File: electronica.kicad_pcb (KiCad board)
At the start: 2 copper layers, 100 x 100 mm, 56 parts, among them J1 Conn_02x02_Counter_Clockwise, J2 Raspberry_Pi_4, J3 Conn_01x12, J4 Conn_01x05, P1 Conn_01x03_Socket, P2 Conn_01x03_Socket, P3 Conn_01x03_Socket, P4 Conn_01x03_Socket, U1 ADS1115 MOD, U2 ULN2003AID

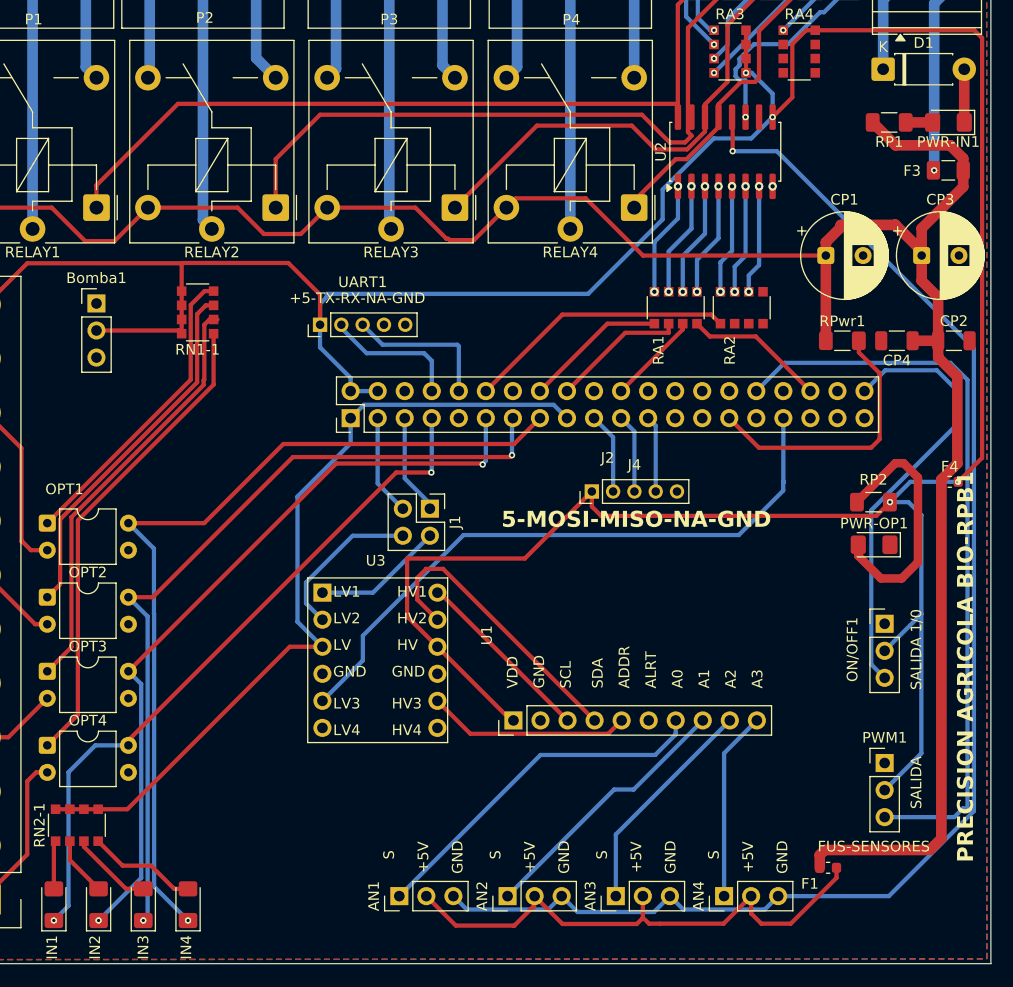
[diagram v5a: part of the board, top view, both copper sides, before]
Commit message: permanece un warning pero no deberia dar problemas4
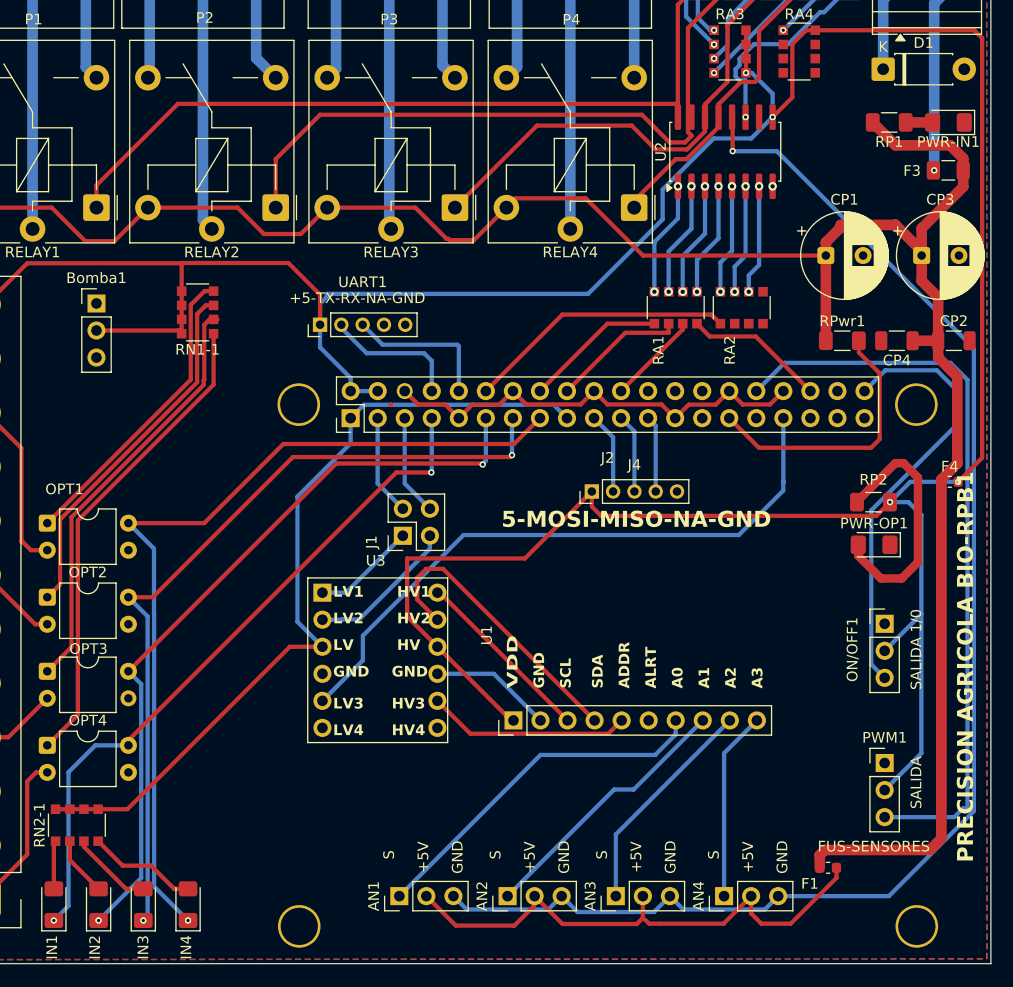
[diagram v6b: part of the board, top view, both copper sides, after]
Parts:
- moved J1 3.59 mm to (84.8, 107.3), turned to 90 degrees
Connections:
- J1 pad 2: Net-(J1-Pin_2) -> IO02-SDA
- J1 pad 3: IO02-SDA -> Net-(J1-Pin_2)
- J2 pad 40: unconnected-(J2-GPIO21/SPI1_SCLK/PCM_DOUT-Pad40) -> IO40
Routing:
- net GND: track 5.00 -> 53.5 mm
- net IO40: track 0.00 -> 41.4 mm
- net (no net): track 41.4 -> 0.00 mm
- net Net-(J1-Pin_1): track 12.3 -> 9.77 mm
- net Net-(J1-Pin_2): track 15.1 -> 14.1 mm

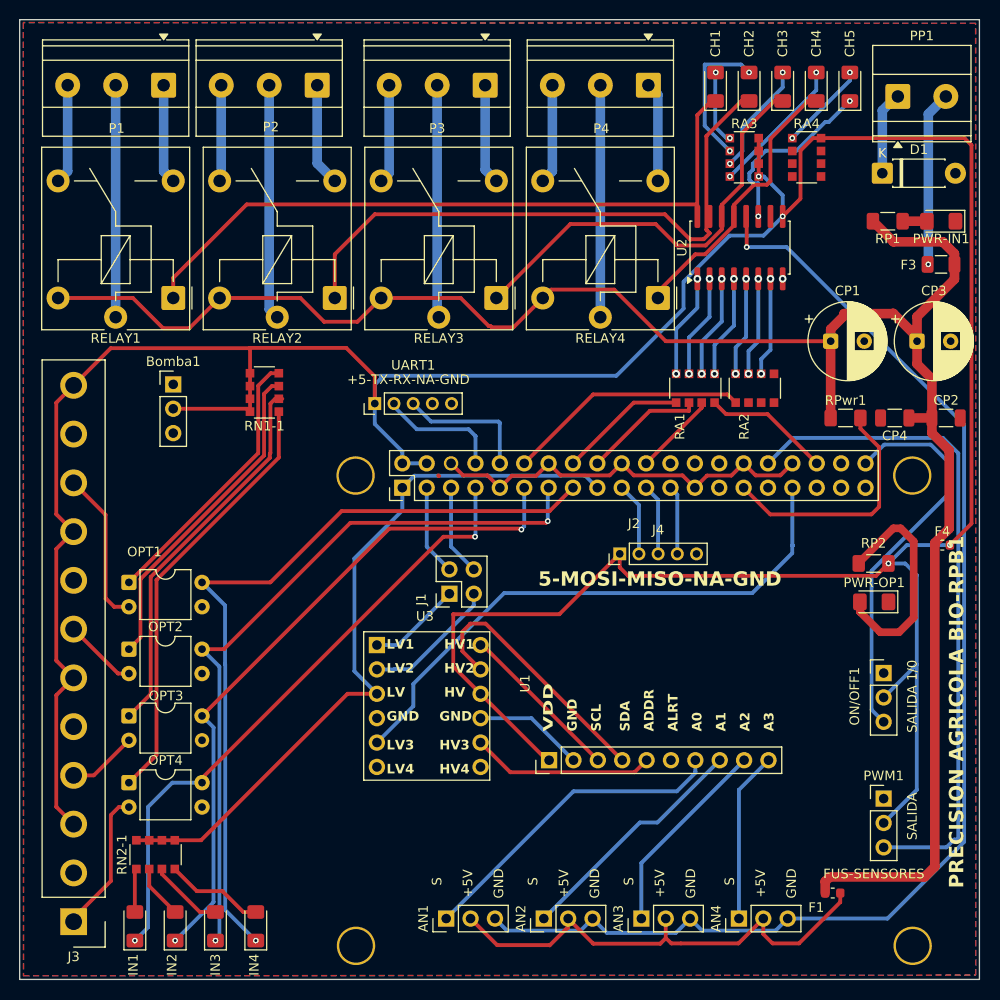
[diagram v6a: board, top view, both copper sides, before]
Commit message: actualizacion de la tarjeta, integracion de otro modulo ads1115 para leer 8 sensores analogos en total e integracion de un ci de opto acopladores de 5 salidas
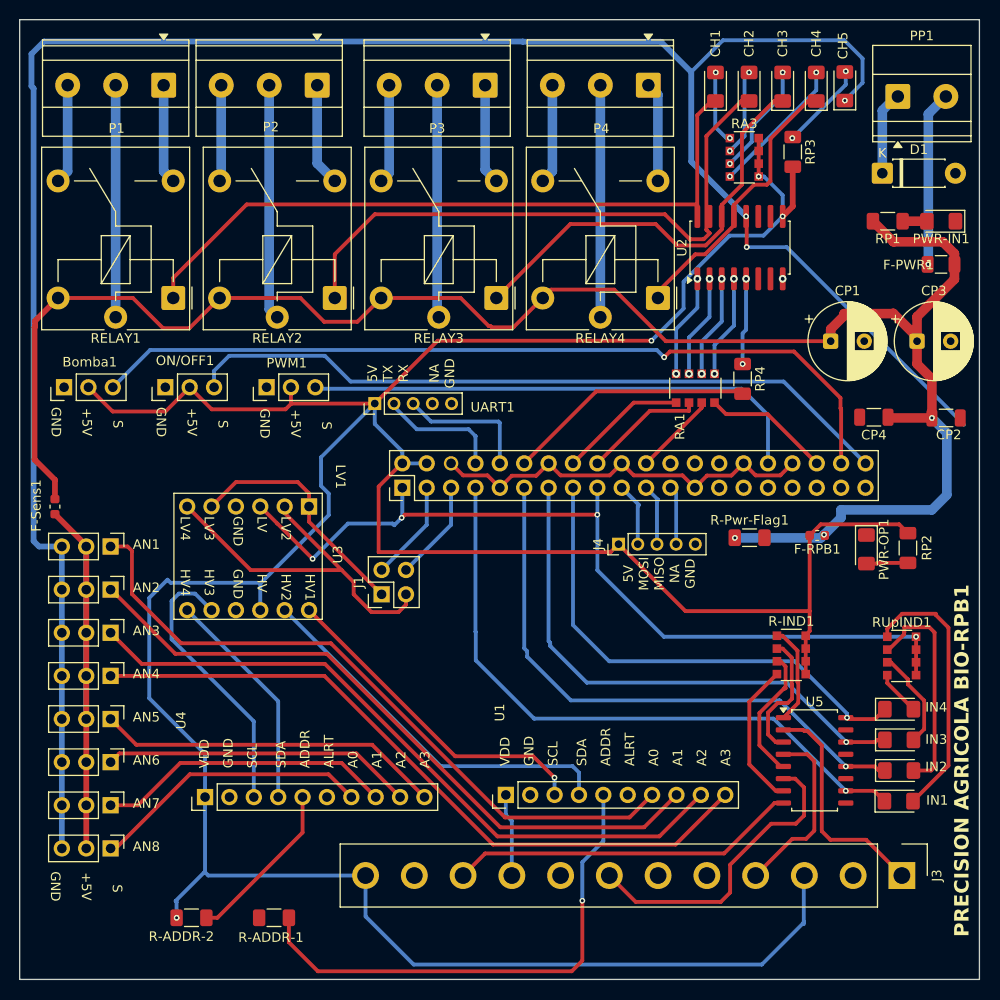
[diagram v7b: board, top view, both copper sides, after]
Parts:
- removed F1, F4: 3A, Fuse:Fuse_0603_1608Metric
- removed OPT1, OPT2, OPT3, OPT4: PC817, Package_DIP:DIP-4_W7.62mm
- removed RA2: 470R, Resistor_SMD:R_Array_Convex_4x1206
- removed RA4: 330, Resistor_SMD:R_Array_Convex_4x1206
- added AN5: Conn_01x03_Socket, Connector_PinHeader_2.54mm:PinHeader_1x03_P2.54mm_Vertical, F.Cu at (49.5, 120.4)
- added AN6: Conn_01x03_Socket, Connector_PinHeader_2.54mm:PinHeader_1x03_P2.54mm_Vertical, F.Cu at (49.5, 124.9)
- added AN7: Conn_01x03_Socket, Connector_PinHeader_2.54mm:PinHeader_1x03_P2.54mm_Vertical, F.Cu at (49.5, 129.4)
- added AN8: Conn_01x03_Socket, Connector_PinHeader_2.54mm:PinHeader_1x03_P2.54mm_Vertical, F.Cu at (49.5, 133.8)
- added F-RPB1: 3A, Fuse:Fuse_0603_1608Metric, F.Cu at (123.1, 101.2)
- added F-Sens1: 3A, Fuse:Fuse_0603_1608Metric, F.Cu at (43.7, 98.2)
- added R-ADDR-1: 10k, Resistor_SMD:R_1206_3216Metric_Pad1.30x1.75mm_HandSolder, F.Cu at (66.5, 141.1)
- added R-ADDR-2: 10k, Resistor_SMD:R_1206_3216Metric_Pad1.30x1.75mm_HandSolder, F.Cu at (57.9, 141.1)
- added RP3: 330, Resistor_SMD:R_1206_3216Metric_Pad1.30x1.75mm_HandSolder, F.Cu at (120.5, 61.3)
- added RP4: 330, Resistor_SMD:R_1206_3216Metric_Pad1.30x1.75mm_HandSolder, F.Cu at (115.3, 84.9)
- added U4: ADS1115 MOD, Connector_PinHeader_2.54mm:ADS1115, F.Cu at (59.3, 128.5)
- added U5: TLP521-4, Package_SO:SOIC-16_4.55x10.3mm_P1.27mm, F.Cu at (122.8, 124.7)
- R-IND1: renamed from RN1-1; value 1k -> 330
- R-Pwr-Flag1: renamed from RPwr1; value 500 -> 1k
- RUpIND1: renamed from RN2-1; value 330 -> 1k
- moved J3 86.4 mm to (131.9, 136.7), turned to -90 degrees
- moved IN1 80.6 mm to (131.6, 128.9), turned to 0 degrees
- moved ON/OFF1 80.6 mm to (55.2, 85.8), turned to 90 degrees
- moved RUpIND1 80.5 mm to (131.9, 113.8), turned to 0 degrees
- moved PWM1 77.3 mm to (65.7, 85.8), turned to 90 degrees
- moved IN2 77.2 mm to (131.6, 125.7), turned to 0 degrees
- moved IN3 73.8 mm to (131.6, 122.5), turned to 0 degrees
- moved IN4 70.7 mm to (131.6, 119.3), turned to 0 degrees
- moved AN4 70.2 mm to (49.5, 115.9), turned to -90 degrees
- moved AN3 62.8 mm to (49.5, 111.4), turned to -90 degrees
- moved R-IND1 61.3 mm to (120.4, 113.7), turned to 0 degrees
- moved AN2 56.7 mm to (49.5, 106.9), turned to -90 degrees
- moved AN1 52.2 mm to (49.5, 102.4), turned to -90 degrees
- moved U3 16.1 mm to (70.2, 98.2), turned to -90 degrees
- moved R-Pwr-Flag1 16.0 mm to (116.0, 101.5)
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- renumbered F3 to F-PWR1
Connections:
- CH5 pad 1: OUT5 -> CONTROL SENORES
- J2 pad 33: ADDR -> unconnected-(J2-GPIO13/PWM1-Pad33)
- J2 pad 38: unconnected-(J2-GPIO20/SPI1_MOSI/PCM_DIN/PWM1-Pad38) -> IO38
- U2 pad 10: OUT6 -> unconnected-(U2-7C-Pad10)
- U2 pad 11: OUT5 -> unconnected-(U2-6C-Pad11)
- U2 pad 6: Net-(RA2-R3.1) -> unconnected-(U2-6B-Pad6)
- U2 pad 7: Net-(RA2-R2.1) -> unconnected-(U2-7B-Pad7)
- U3 pad 10: Net-(U1-ADDR) -> Net-(U3-HV3)
- U3 pad 11: unconnected-(U3-LV4-Pad11) -> Net-(J1-Pin_2)
- U3 pad 12: unconnected-(U3-HV4-Pad12) -> Net-(U3-HV4)
- U3 pad 9: ADDR -> Net-(J1-Pin_1)
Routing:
- net CONTROL SENORES: track 132.5 -> 232.2 mm, vias 1 -> 3
- net IO38: track 0.00 -> 86.8 mm, vias 0 -> 1
- net ADDR: track 59.7 -> 0.00 mm
- net AN3: track 17.8 -> 73.5 mm
- net AN2: track 20.9 -> 72.1 mm
- net AN1: track 25.2 -> 70.6 mm
- net AN0: track 33.6 -> 71.8 mm
- net AN4: track 0.00 -> 36.1 mm
- net Net-(R-IND1-R1.1): track 45.1 -> 10.5 mm
- net Net-(U1-ADDR): track 19.1 -> 53.0 mm, vias 0 -> 1
- net IO40: track 41.4 -> 74.9 mm
- net AN5: track 0.00 -> 32.4 mm
- net AN6: track 0.00 -> 30.9 mm
- net IO22: track 82.4 -> 51.7 mm
- net AN7: track 0.00 -> 29.3 mm
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- removed copper zone on B.Cu, net GND
- removed copper zone on F.Cu, net GND
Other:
- board text added: "5V MOSI MISO NA GND"
- board text added: "5V TX RX NA GND"
- board text removed: "5-MOSI-MISO-NA-GND"

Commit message: zona de gnds
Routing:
- net /5V: track 357.3 -> 394.0 mm
- net CONTROL SENORES: track 232.2 -> 198.7 mm, vias 3 -> 2
- net GND: track 41.9 -> 12.3 mm
- net IO05: track 0.00 -> 6.10 mm
- added copper zone on B.Cu, net GND
- added copper zone on F.Cu, net GND
